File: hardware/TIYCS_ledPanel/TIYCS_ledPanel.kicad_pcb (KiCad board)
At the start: 2 copper layers, 100 x 100 mm, 74 parts

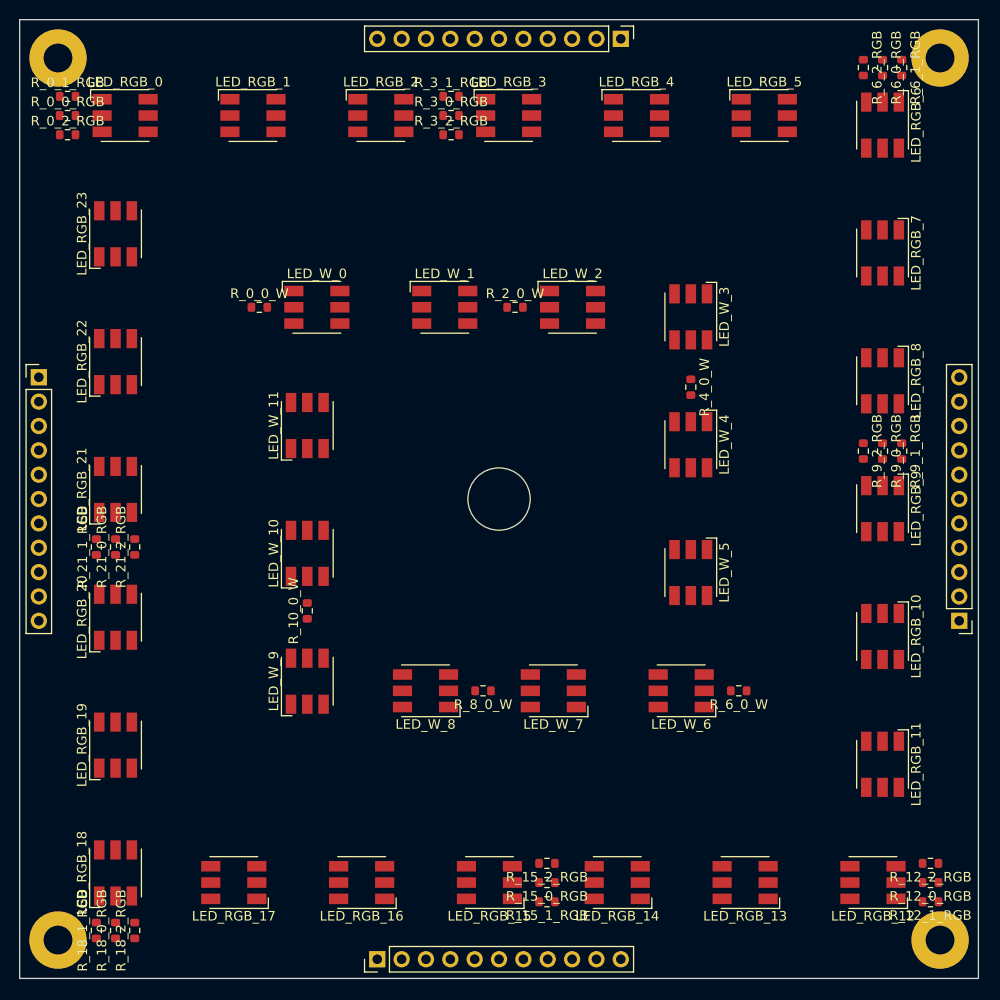
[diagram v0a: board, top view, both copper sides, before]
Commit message: More LED-rings, 36RGB and 18W
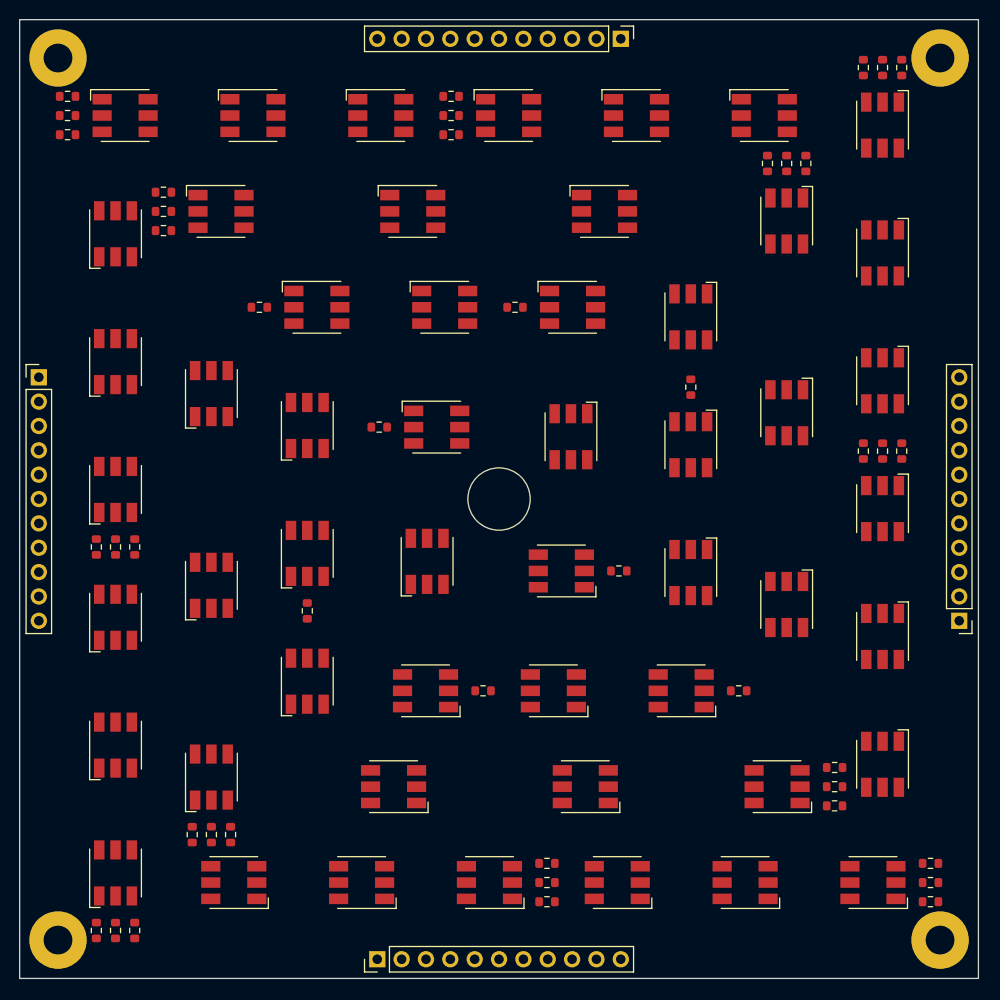
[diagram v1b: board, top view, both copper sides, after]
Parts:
- removed the R_0_0_RGB at (-45.0, -40.0)
- removed the R_0_0_W at (-25.0, -20.0)
- removed the R_0_1_RGB at (-45.0, -42.0)
- removed the R_0_2_RGB at (-45.0, -38.0)
- removed the R_10_0_W at (-20.0, 11.7)
- removed the R_12_0_RGB at (45.0, 40.0)
- removed the R_12_1_RGB at (45.0, 42.0)
- removed the R_12_2_RGB at (45.0, 38.0)
- removed the R_15_0_RGB at (5.00, 40.0)
- removed the R_15_1_RGB at (5.00, 42.0)
- removed the R_15_2_RGB at (5.00, 38.0)
- removed the R_18_0_RGB at (-40.0, 45.0)
- removed the R_18_1_RGB at (-42.0, 45.0)
- removed the R_18_2_RGB at (-38.0, 45.0)
- removed the R_21_0_RGB at (-40.0, 5.00)
- removed the R_21_1_RGB at (-42.0, 5.00)
- removed the R_21_2_RGB at (-38.0, 5.00)
- removed the R_2_0_W at (1.67, -20.0)
- removed the R_3_0_RGB at (-5.00, -40.0)
- removed the R_3_1_RGB at (-5.00, -42.0)
- removed the R_3_2_RGB at (-5.00, -38.0)
- removed the R_4_0_W at (20.0, -11.7)
- removed the R_6_0_RGB at (40.0, -45.0)
- removed the R_6_0_W at (25.0, 20.0)
- removed the R_6_1_RGB at (42.0, -45.0)
- removed the R_6_2_RGB at (38.0, -45.0)
- removed the R_8_0_W at (-1.67, 20.0)
- removed the R_9_0_RGB at (40.0, -5.00)
- removed the R_9_1_RGB at (42.0, -5.00)
- removed the R_9_2_RGB at (38.0, -5.00)
- removed the mainConn_[-1, 0] at (-48.0, -12.7)
- removed the mainConn_[0, -1] at (12.7, -48.0)
- removed the mainConn_[0, 1] at (-12.7, 48.0)
- removed the mainConn_[1, 0] at (48.0, 12.7)
- added LED_RGB2_0: LED_RGB_5050-6, LED_SMD:LED_RGB_5050-6, F.Cu at (-29.0, -30.0)
- added LED_RGB2_1: LED_RGB_5050-6, LED_SMD:LED_RGB_5050-6, F.Cu at (-9.00, -30.0)
- added LED_RGB2_10: LED_RGB_5050-6, LED_SMD:LED_RGB_5050-6, F.Cu at (-30.0, 9.00)
- added LED_RGB2_11: LED_RGB_5050-6, LED_SMD:LED_RGB_5050-6, F.Cu at (-30.0, -11.0)
- added LED_RGB2_2: LED_RGB_5050-6, LED_SMD:LED_RGB_5050-6, F.Cu at (11.0, -30.0)
- added LED_RGB2_3: LED_RGB_5050-6, LED_SMD:LED_RGB_5050-6, F.Cu at (30.0, -29.0)
- added LED_RGB2_4: LED_RGB_5050-6, LED_SMD:LED_RGB_5050-6, F.Cu at (30.0, -9.00)
- added LED_RGB2_5: LED_RGB_5050-6, LED_SMD:LED_RGB_5050-6, F.Cu at (30.0, 11.0)
- added LED_RGB2_6: LED_RGB_5050-6, LED_SMD:LED_RGB_5050-6, F.Cu at (29.0, 30.0)
- added LED_RGB2_7: LED_RGB_5050-6, LED_SMD:LED_RGB_5050-6, F.Cu at (9.00, 30.0)
- added LED_RGB2_8: LED_RGB_5050-6, LED_SMD:LED_RGB_5050-6, F.Cu at (-11.0, 30.0)
- added LED_RGB2_9: LED_RGB_5050-6, LED_SMD:LED_RGB_5050-6, F.Cu at (-30.0, 29.0)
- added LED_W2_0: LED_RGB_5050-6, LED_SMD:LED_RGB_5050-6, F.Cu at (-6.50, -7.50)
- added LED_W2_1: LED_RGB_5050-6, LED_SMD:LED_RGB_5050-6, F.Cu at (7.50, -6.50)
- added LED_W2_2: LED_RGB_5050-6, LED_SMD:LED_RGB_5050-6, F.Cu at (6.50, 7.50)
- added LED_W2_3: LED_RGB_5050-6, LED_SMD:LED_RGB_5050-6, F.Cu at (-7.50, 6.50)
- added R_0_0_RGB: R_0603_1608Metric, Resistor_SMD:R_0603_1608Metric, F.Cu at (-45.0, -40.0)
- added R_0_0_RGB: R_0603_1608Metric, Resistor_SMD:R_0603_1608Metric, F.Cu at (-35.0, -30.0)
- added R_0_0_W: R_0603_1608Metric, Resistor_SMD:R_0603_1608Metric, F.Cu at (-25.0, -20.0)
- added R_0_0_W2: R_0603_1608Metric, Resistor_SMD:R_0603_1608Metric, F.Cu at (-12.5, -7.50)
- added R_0_1_RGB: R_0603_1608Metric, Resistor_SMD:R_0603_1608Metric, F.Cu at (-45.0, -42.0)
- added R_0_1_RGB: R_0603_1608Metric, Resistor_SMD:R_0603_1608Metric, F.Cu at (-35.0, -32.0)
- added R_0_2_RGB: R_0603_1608Metric, Resistor_SMD:R_0603_1608Metric, F.Cu at (-45.0, -38.0)
- added R_0_2_RGB: R_0603_1608Metric, Resistor_SMD:R_0603_1608Metric, F.Cu at (-35.0, -28.0)
- added R_10_0_W: R_0603_1608Metric, Resistor_SMD:R_0603_1608Metric, F.Cu at (-20.0, 11.7)
- added R_12_0_RGB: R_0603_1608Metric, Resistor_SMD:R_0603_1608Metric, F.Cu at (45.0, 40.0)
- added R_12_1_RGB: R_0603_1608Metric, Resistor_SMD:R_0603_1608Metric, F.Cu at (45.0, 42.0)
- added R_12_2_RGB: R_0603_1608Metric, Resistor_SMD:R_0603_1608Metric, F.Cu at (45.0, 38.0)
- added R_15_0_RGB: R_0603_1608Metric, Resistor_SMD:R_0603_1608Metric, F.Cu at (5.00, 40.0)
- added R_15_1_RGB: R_0603_1608Metric, Resistor_SMD:R_0603_1608Metric, F.Cu at (5.00, 42.0)
- added R_15_2_RGB: R_0603_1608Metric, Resistor_SMD:R_0603_1608Metric, F.Cu at (5.00, 38.0)
- added R_18_0_RGB: R_0603_1608Metric, Resistor_SMD:R_0603_1608Metric, F.Cu at (-40.0, 45.0)
- added R_18_1_RGB: R_0603_1608Metric, Resistor_SMD:R_0603_1608Metric, F.Cu at (-42.0, 45.0)
- added R_18_2_RGB: R_0603_1608Metric, Resistor_SMD:R_0603_1608Metric, F.Cu at (-38.0, 45.0)
- added R_21_0_RGB: R_0603_1608Metric, Resistor_SMD:R_0603_1608Metric, F.Cu at (-40.0, 5.00)
- added R_21_1_RGB: R_0603_1608Metric, Resistor_SMD:R_0603_1608Metric, F.Cu at (-42.0, 5.00)
- added R_21_2_RGB: R_0603_1608Metric, Resistor_SMD:R_0603_1608Metric, F.Cu at (-38.0, 5.00)
- added R_2_0_W: R_0603_1608Metric, Resistor_SMD:R_0603_1608Metric, F.Cu at (1.67, -20.0)
- added R_2_0_W2: R_0603_1608Metric, Resistor_SMD:R_0603_1608Metric, F.Cu at (12.5, 7.50)
- added R_3_0_RGB: R_0603_1608Metric, Resistor_SMD:R_0603_1608Metric, F.Cu at (-5.00, -40.0)
- added R_3_0_RGB: R_0603_1608Metric, Resistor_SMD:R_0603_1608Metric, F.Cu at (30.0, -35.0)
- added R_3_1_RGB: R_0603_1608Metric, Resistor_SMD:R_0603_1608Metric, F.Cu at (-5.00, -42.0)
- added R_3_1_RGB: R_0603_1608Metric, Resistor_SMD:R_0603_1608Metric, F.Cu at (32.0, -35.0)
- added R_3_2_RGB: R_0603_1608Metric, Resistor_SMD:R_0603_1608Metric, F.Cu at (28.0, -35.0)
- added R_3_2_RGB: R_0603_1608Metric, Resistor_SMD:R_0603_1608Metric, F.Cu at (-5.00, -38.0)
- added R_4_0_W: R_0603_1608Metric, Resistor_SMD:R_0603_1608Metric, F.Cu at (20.0, -11.7)
- added R_6_0_RGB: R_0603_1608Metric, Resistor_SMD:R_0603_1608Metric, F.Cu at (35.0, 30.0)
- added R_6_0_RGB: R_0603_1608Metric, Resistor_SMD:R_0603_1608Metric, F.Cu at (40.0, -45.0)
- added R_6_0_W: R_0603_1608Metric, Resistor_SMD:R_0603_1608Metric, F.Cu at (25.0, 20.0)
- added R_6_1_RGB: R_0603_1608Metric, Resistor_SMD:R_0603_1608Metric, F.Cu at (42.0, -45.0)
- added R_6_1_RGB: R_0603_1608Metric, Resistor_SMD:R_0603_1608Metric, F.Cu at (35.0, 32.0)
- added R_6_2_RGB: R_0603_1608Metric, Resistor_SMD:R_0603_1608Metric, F.Cu at (38.0, -45.0)
- added R_6_2_RGB: R_0603_1608Metric, Resistor_SMD:R_0603_1608Metric, F.Cu at (35.0, 28.0)
- added R_8_0_W: R_0603_1608Metric, Resistor_SMD:R_0603_1608Metric, F.Cu at (-1.67, 20.0)
- added R_9_0_RGB: R_0603_1608Metric, Resistor_SMD:R_0603_1608Metric, F.Cu at (40.0, -5.00)
- added R_9_0_RGB: R_0603_1608Metric, Resistor_SMD:R_0603_1608Metric, F.Cu at (-30.0, 35.0)
- added R_9_1_RGB: R_0603_1608Metric, Resistor_SMD:R_0603_1608Metric, F.Cu at (-32.0, 35.0)
- added R_9_1_RGB: R_0603_1608Metric, Resistor_SMD:R_0603_1608Metric, F.Cu at (42.0, -5.00)
- added R_9_2_RGB: R_0603_1608Metric, Resistor_SMD:R_0603_1608Metric, F.Cu at (38.0, -5.00)
- added R_9_2_RGB: R_0603_1608Metric, Resistor_SMD:R_0603_1608Metric, F.Cu at (-28.0, 35.0)
- added mainConn_[-1, 0]: PinHeader_1x11_P2.54mm_Vertical, Connector_PinHeader_2.54mm:PinHeader_1x11_P2.54mm_Vertical, F.Cu at (-48.0, -12.7)
- added mainConn_[0, -1]: PinHeader_1x11_P2.54mm_Vertical, Connector_PinHeader_2.54mm:PinHeader_1x11_P2.54mm_Vertical, F.Cu at (12.7, -48.0)
- added mainConn_[0, 1]: PinHeader_1x11_P2.54mm_Vertical, Connector_PinHeader_2.54mm:PinHeader_1x11_P2.54mm_Vertical, F.Cu at (-12.7, 48.0)
- added mainConn_[1, 0]: PinHeader_1x11_P2.54mm_Vertical, Connector_PinHeader_2.54mm:PinHeader_1x11_P2.54mm_Vertical, F.Cu at (48.0, 12.7)
- H_0, H_1, H_2, H_3: footprint MountingHole_3mm_Pad -> MountingHole:MountingHole_3mm_Pad
- LED_RGB_0, LED_RGB_1, LED_RGB_10, LED_RGB_11, LED_RGB_12, LED_RGB_13, LED_RGB_14, LED_RGB_15, LED_RGB_16, LED_RGB_17, LED_RGB_18, LED_RGB_19, LED_RGB_2, LED_RGB_20, LED_RGB_21, LED_RGB_22, LED_RGB_23, LED_RGB_3, LED_RGB_4, LED_RGB_5, LED_RGB_6, LED_RGB_7, LED_RGB_8, LED_RGB_9, LED_W_0, LED_W_1, LED_W_10, LED_W_11, LED_W_2, LED_W_3, LED_W_4, LED_W_5, LED_W_6, LED_W_7, LED_W_8, LED_W_9: footprint LED_RGB_5050-6 -> LED_SMD:LED_RGB_5050-6

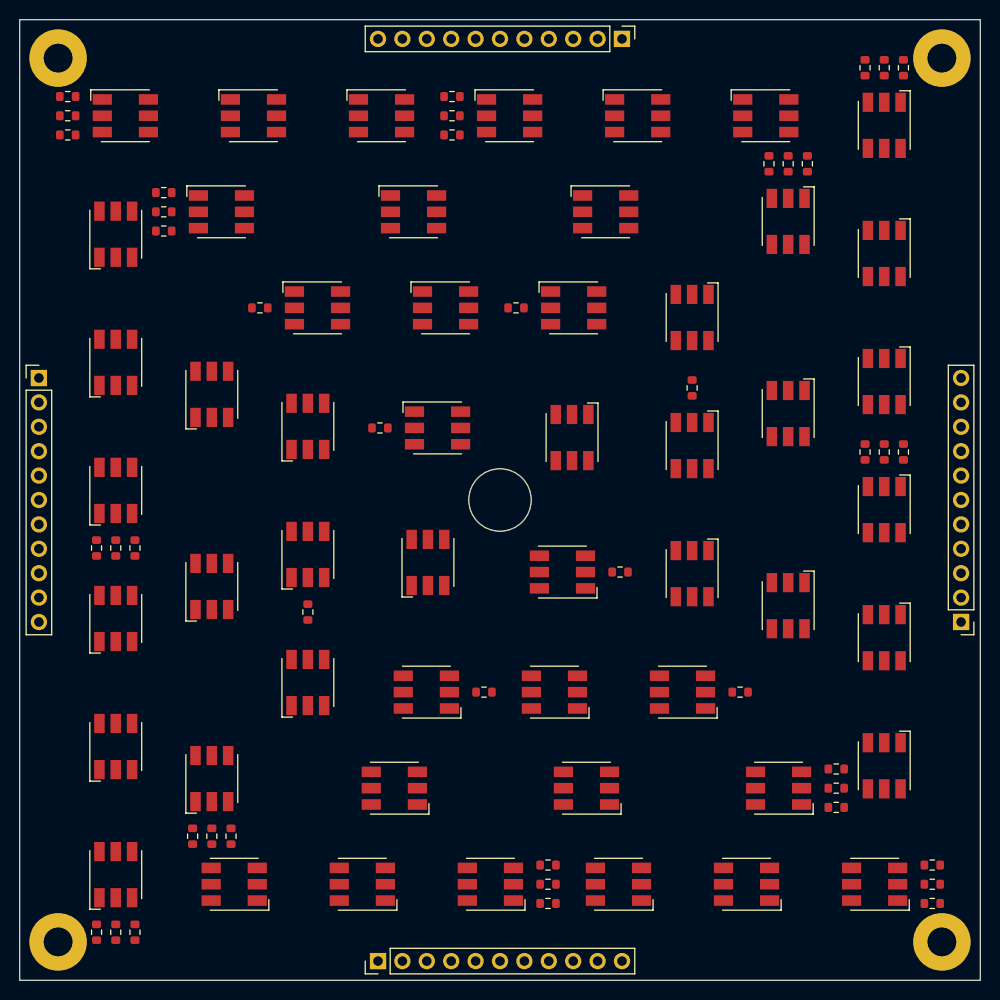
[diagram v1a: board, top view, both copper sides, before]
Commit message: Added extra header for connection to motherboard
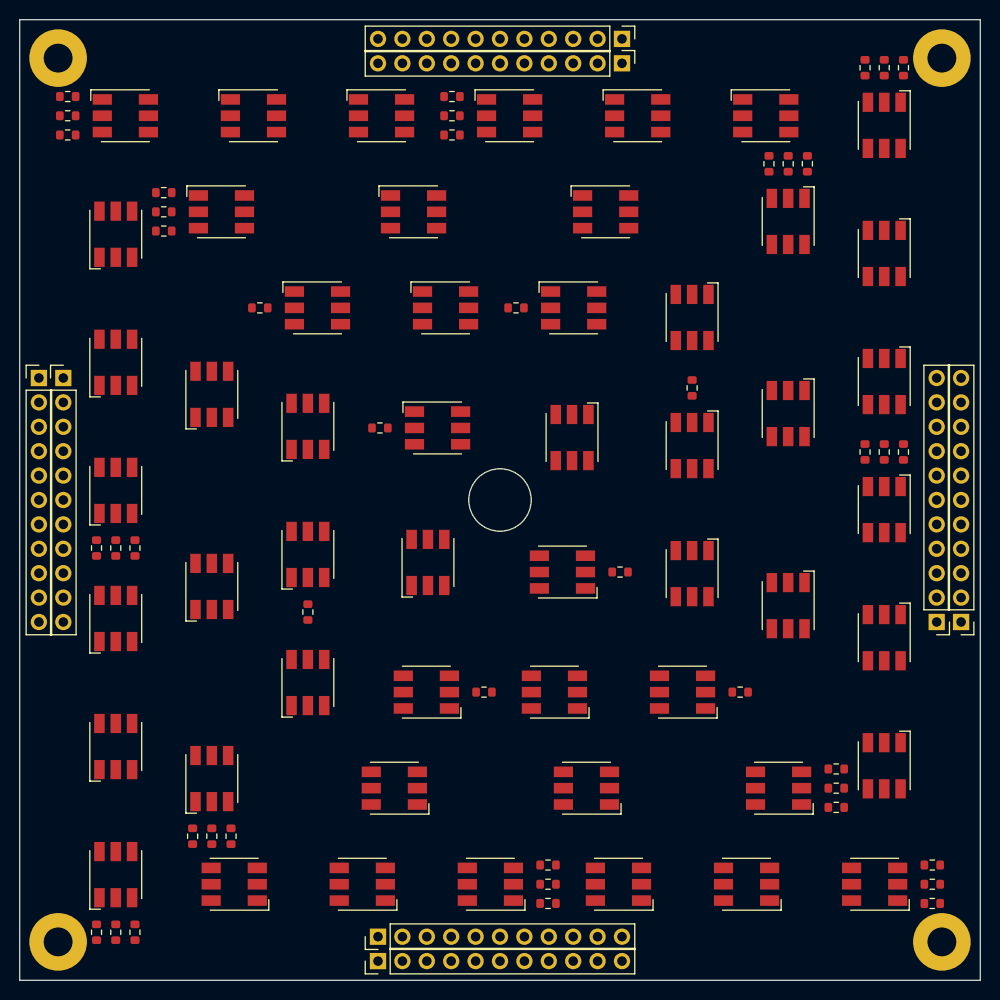
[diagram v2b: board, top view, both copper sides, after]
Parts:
- removed the R_0_0_RGB at (-45.0, -40.0)
- removed the R_0_0_RGB at (-35.0, -30.0)
- removed the R_0_0_W at (-25.0, -20.0)
- removed the R_0_1_RGB at (-45.0, -42.0)
- removed the R_0_1_RGB at (-35.0, -32.0)
- removed the R_0_2_RGB at (-45.0, -38.0)
- removed the R_0_2_RGB at (-35.0, -28.0)
- removed the R_10_0_W at (-20.0, 11.7)
- removed the R_12_0_RGB at (45.0, 40.0)
- removed the R_12_1_RGB at (45.0, 42.0)
- removed the R_12_2_RGB at (45.0, 38.0)
- removed the R_15_0_RGB at (5.00, 40.0)
- removed the R_15_1_RGB at (5.00, 42.0)
- removed the R_15_2_RGB at (5.00, 38.0)
- removed the R_18_0_RGB at (-40.0, 45.0)
- removed the R_18_1_RGB at (-42.0, 45.0)
- removed the R_18_2_RGB at (-38.0, 45.0)
- removed the R_21_0_RGB at (-40.0, 5.00)
- removed the R_21_1_RGB at (-42.0, 5.00)
- removed the R_21_2_RGB at (-38.0, 5.00)
- removed the R_2_0_W at (1.67, -20.0)
- removed the R_3_0_RGB at (-5.00, -40.0)
- removed the R_3_0_RGB at (30.0, -35.0)
- removed the R_3_1_RGB at (-5.00, -42.0)
- removed the R_3_1_RGB at (32.0, -35.0)
- removed the R_3_2_RGB at (28.0, -35.0)
- removed the R_3_2_RGB at (-5.00, -38.0)
- removed the R_4_0_W at (20.0, -11.7)
- removed the R_6_0_RGB at (35.0, 30.0)
- removed the R_6_0_RGB at (40.0, -45.0)
- removed the R_6_0_W at (25.0, 20.0)
- removed the R_6_1_RGB at (42.0, -45.0)
- removed the R_6_1_RGB at (35.0, 32.0)
- removed the R_6_2_RGB at (38.0, -45.0)
- removed the R_6_2_RGB at (35.0, 28.0)
- removed the R_8_0_W at (-1.67, 20.0)
- removed the R_9_0_RGB at (40.0, -5.00)
- removed the R_9_0_RGB at (-30.0, 35.0)
- removed the R_9_1_RGB at (-32.0, 35.0)
- removed the R_9_1_RGB at (42.0, -5.00)
- removed the R_9_2_RGB at (38.0, -5.00)
- removed the R_9_2_RGB at (-28.0, 35.0)
- added R_0_0_RGB: R_0603_1608Metric, R_0603_1608Metric, F.Cu at (-45.0, -40.0)
- added R_0_0_RGB: R_0603_1608Metric, R_0603_1608Metric, F.Cu at (-35.0, -30.0)
- added R_0_0_W: R_0603_1608Metric, R_0603_1608Metric, F.Cu at (-25.0, -20.0)
- added R_0_1_RGB: R_0603_1608Metric, R_0603_1608Metric, F.Cu at (-35.0, -32.0)
- added R_0_1_RGB: R_0603_1608Metric, R_0603_1608Metric, F.Cu at (-45.0, -42.0)
- added R_0_2_RGB: R_0603_1608Metric, R_0603_1608Metric, F.Cu at (-35.0, -28.0)
- added R_0_2_RGB: R_0603_1608Metric, R_0603_1608Metric, F.Cu at (-45.0, -38.0)
- added R_10_0_W: R_0603_1608Metric, R_0603_1608Metric, F.Cu at (-20.0, 11.7)
- added R_12_0_RGB: R_0603_1608Metric, R_0603_1608Metric, F.Cu at (45.0, 40.0)
- added R_12_1_RGB: R_0603_1608Metric, R_0603_1608Metric, F.Cu at (45.0, 42.0)
- added R_12_2_RGB: R_0603_1608Metric, R_0603_1608Metric, F.Cu at (45.0, 38.0)
- added R_15_0_RGB: R_0603_1608Metric, R_0603_1608Metric, F.Cu at (5.00, 40.0)
- added R_15_1_RGB: R_0603_1608Metric, R_0603_1608Metric, F.Cu at (5.00, 42.0)
- added R_15_2_RGB: R_0603_1608Metric, R_0603_1608Metric, F.Cu at (5.00, 38.0)
- added R_18_0_RGB: R_0603_1608Metric, R_0603_1608Metric, F.Cu at (-40.0, 45.0)
- added R_18_1_RGB: R_0603_1608Metric, R_0603_1608Metric, F.Cu at (-42.0, 45.0)
- added R_18_2_RGB: R_0603_1608Metric, R_0603_1608Metric, F.Cu at (-38.0, 45.0)
- added R_21_0_RGB: R_0603_1608Metric, R_0603_1608Metric, F.Cu at (-40.0, 5.00)
- added R_21_1_RGB: R_0603_1608Metric, R_0603_1608Metric, F.Cu at (-42.0, 5.00)
- added R_21_2_RGB: R_0603_1608Metric, R_0603_1608Metric, F.Cu at (-38.0, 5.00)
- added R_2_0_W: R_0603_1608Metric, R_0603_1608Metric, F.Cu at (1.67, -20.0)
- added R_3_0_RGB: R_0603_1608Metric, R_0603_1608Metric, F.Cu at (-5.00, -40.0)
- added R_3_0_RGB: R_0603_1608Metric, R_0603_1608Metric, F.Cu at (30.0, -35.0)
- added R_3_1_RGB: R_0603_1608Metric, R_0603_1608Metric, F.Cu at (-5.00, -42.0)
- added R_3_1_RGB: R_0603_1608Metric, R_0603_1608Metric, F.Cu at (32.0, -35.0)
- added R_3_2_RGB: R_0603_1608Metric, R_0603_1608Metric, F.Cu at (28.0, -35.0)
- added R_3_2_RGB: R_0603_1608Metric, R_0603_1608Metric, F.Cu at (-5.00, -38.0)
- added R_4_0_W: R_0603_1608Metric, R_0603_1608Metric, F.Cu at (20.0, -11.7)
- added R_6_0_RGB: R_0603_1608Metric, R_0603_1608Metric, F.Cu at (35.0, 30.0)
- added R_6_0_RGB: R_0603_1608Metric, R_0603_1608Metric, F.Cu at (40.0, -45.0)
- added R_6_0_W: R_0603_1608Metric, R_0603_1608Metric, F.Cu at (25.0, 20.0)
- added R_6_1_RGB: R_0603_1608Metric, R_0603_1608Metric, F.Cu at (35.0, 32.0)
- added R_6_1_RGB: R_0603_1608Metric, R_0603_1608Metric, F.Cu at (42.0, -45.0)
- added R_6_2_RGB: R_0603_1608Metric, R_0603_1608Metric, F.Cu at (38.0, -45.0)
- added R_6_2_RGB: R_0603_1608Metric, R_0603_1608Metric, F.Cu at (35.0, 28.0)
- added R_8_0_W: R_0603_1608Metric, R_0603_1608Metric, F.Cu at (-1.67, 20.0)
- added R_9_0_RGB: R_0603_1608Metric, R_0603_1608Metric, F.Cu at (-30.0, 35.0)
- added R_9_0_RGB: R_0603_1608Metric, R_0603_1608Metric, F.Cu at (40.0, -5.00)
- added R_9_1_RGB: R_0603_1608Metric, R_0603_1608Metric, F.Cu at (-32.0, 35.0)
- added R_9_1_RGB: R_0603_1608Metric, R_0603_1608Metric, F.Cu at (42.0, -5.00)
- added R_9_2_RGB: R_0603_1608Metric, R_0603_1608Metric, F.Cu at (-28.0, 35.0)
- added R_9_2_RGB: R_0603_1608Metric, R_0603_1608Metric, F.Cu at (38.0, -5.00)
- added mainConn_0_1: PinHeader_1x11_P2.54mm_Vertical, PinHeader_1x11_P2.54mm_Vertical, F.Cu at (-45.5, -12.7)
- added mainConn_1_1: PinHeader_1x11_P2.54mm_Vertical, PinHeader_1x11_P2.54mm_Vertical, F.Cu at (12.7, -45.5)
- added mainConn_2_1: PinHeader_1x11_P2.54mm_Vertical, PinHeader_1x11_P2.54mm_Vertical, F.Cu at (45.5, 12.7)
- added mainConn_3_1: PinHeader_1x11_P2.54mm_Vertical, PinHeader_1x11_P2.54mm_Vertical, F.Cu at (-12.7, 45.5)
- H_0, H_1, H_2, H_3: footprint MountingHole:MountingHole_3mm_Pad -> MountingHole_3mm_Pad
- LED_RGB2_0, LED_RGB2_1, LED_RGB2_10, LED_RGB2_11, LED_RGB2_2, LED_RGB2_3, LED_RGB2_4, LED_RGB2_5, LED_RGB2_6, LED_RGB2_7, LED_RGB2_8, LED_RGB2_9, LED_RGB_0, LED_RGB_1, LED_RGB_10, LED_RGB_11, LED_RGB_12, LED_RGB_13, LED_RGB_14, LED_RGB_15, LED_RGB_16, LED_RGB_17, LED_RGB_18, LED_RGB_19, LED_RGB_2, LED_RGB_20, LED_RGB_21, LED_RGB_22, LED_RGB_23, LED_RGB_3, LED_RGB_4, LED_RGB_5, LED_RGB_6, LED_RGB_7, LED_RGB_8, LED_RGB_9, LED_W2_0, LED_W2_1, LED_W2_2, LED_W2_3, LED_W_0, LED_W_1, LED_W_10, LED_W_11, LED_W_2, LED_W_3, LED_W_4, LED_W_5, LED_W_6, LED_W_7, LED_W_8, LED_W_9: footprint LED_SMD:LED_RGB_5050-6 -> LED_RGB_5050-6
- R_0_0_W2, R_2_0_W2: footprint Resistor_SMD:R_0603_1608Metric -> R_0603_1608Metric
- mainConn_0_0: renamed from mainConn_[-1, 0]; footprint Connector_PinHeader_2.54mm:PinHeader_1x11_P2.54mm_Vertical -> PinHeader_1x11_P2.54mm_Vertical
- mainConn_1_0: renamed from mainConn_[0, -1]; footprint Connector_PinHeader_2.54mm:PinHeader_1x11_P2.54mm_Vertical -> PinHeader_1x11_P2.54mm_Vertical
- mainConn_2_0: renamed from mainConn_[1, 0]; footprint Connector_PinHeader_2.54mm:PinHeader_1x11_P2.54mm_Vertical -> PinHeader_1x11_P2.54mm_Vertical
- mainConn_3_0: renamed from mainConn_[0, 1]; footprint Connector_PinHeader_2.54mm:PinHeader_1x11_P2.54mm_Vertical -> PinHeader_1x11_P2.54mm_Vertical
